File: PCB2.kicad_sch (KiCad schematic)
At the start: 8 parts, among them J701 Conn_02x03_Odd_Even

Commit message: Finish 0.1.0 design
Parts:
- J701: LCSC (none) -> C65114
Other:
- title: SH-wg -> Sailor Hat WiFi Gateway
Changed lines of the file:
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@@
   (paper "A4")
   (title_block
-    (title "SH-wg")
+    (title "Sailor Hat WiFi Gateway")
     (date "2022-01-25")
     (rev "0.1.0")
@@
     )
     (property "Datasheet" "~" (id 3) (at 132.08 60.96 0)
+      (effects (font (size 1.27 1.27)) hide)
+    )
+    (property "LCSC" "C65114" (id 4) (at 132.08 60.96 0)
       (effects (font (size 1.27 1.27)) hide)
     )
@@
     (pin "6")
   )
-  (symbol (lib_id "SH-ESP32-mini:+3V3_1") (at 147.32 55.88 0) (unit 1)
+  (symbol (lib_id "SH-wg:+3V3_1") (at 147.32 55.88 0) (unit 1)
     (in_bom yes) (on_board yes) (fields_autoplaced)
     (property "Reference" "#PWR0703" (id 0) (at 147.32 59.69 0)
@@
     (pin "1")
   )
-  (symbol (lib_id "SH-ESP32-mini:+3V3_1") (at 58.42 43.18 0) (unit 1)
+  (symbol (lib_id "SH-wg:+3V3_1") (at 58.42 43.18 0) (unit 1)
     (in_bom yes) (on_board yes) (fields_autoplaced)
     (property "Reference" "#PWR0702" (id 0) (at 58.42 46.99 0)

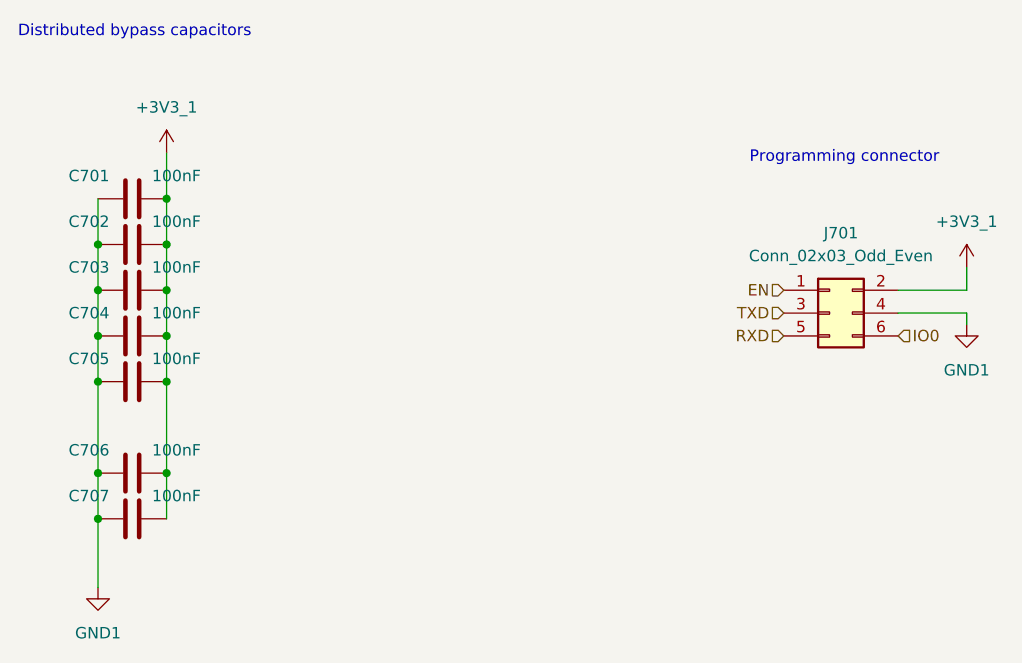
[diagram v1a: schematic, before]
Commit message: Update the design based on the test results
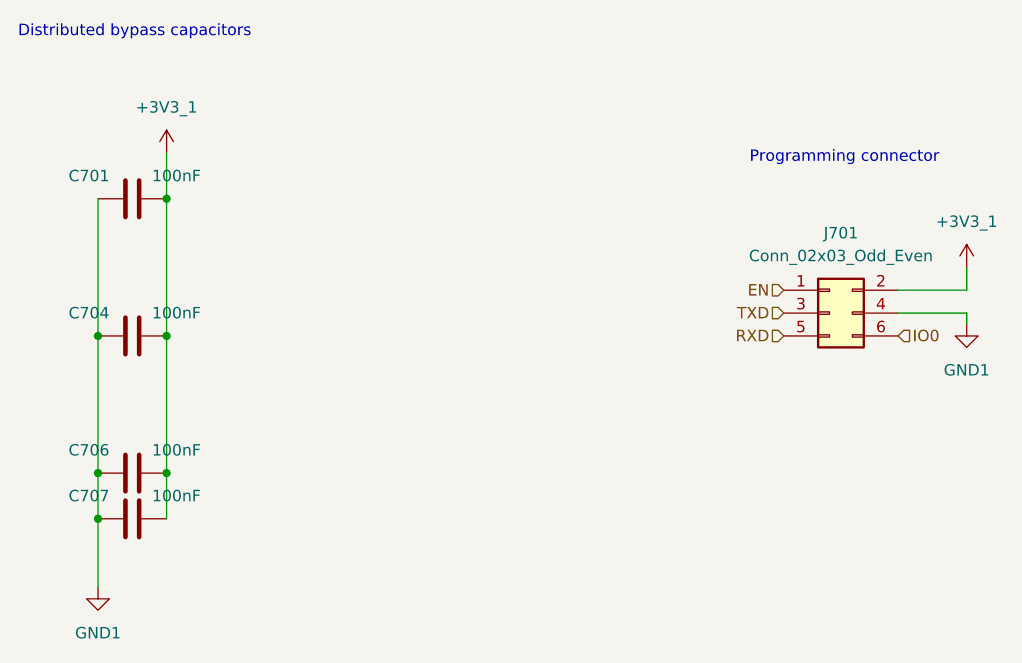
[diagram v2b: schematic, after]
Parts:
- removed C702, C703, C705: 100nF, Capacitor_SMD:C_0402_1005Metric, symbol Device:C
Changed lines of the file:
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@@
   (junction (at 50.8 63.5) (diameter 0) (color 0 0 0 0)
   )
-  (junction (at 50.8 68.58) (diameter 0) (color 0 0 0 0)
-  )
-  (junction (at 50.8 58.42) (diameter 0) (color 0 0 0 0)
-  )
   (junction (at 58.42 48.26) (diameter 0) (color 0 0 0 0)
-  )
-  (junction (at 58.42 53.34) (diameter 0) (color 0 0 0 0)
-  )
-  (junction (at 58.42 68.58) (diameter 0) (color 0 0 0 0)
   )
   (junction (at 50.8 78.74) (diameter 0) (color 0 0 0 0)
@@
   (junction (at 58.42 78.74) (diameter 0) (color 0 0 0 0)
   )
-  (junction (at 50.8 53.34) (diameter 0) (color 0 0 0 0)
-  )
   (junction (at 58.42 63.5) (diameter 0) (color 0 0 0 0)
   )
-  (junction (at 58.42 58.42) (diameter 0) (color 0 0 0 0)
-  )
-  (wire (pts (xy 50.8 58.42) (xy 50.8 63.5))
-    (stroke (width 0) (type default) (color 0 0 0 0))
-  )
-  (wire (pts (xy 58.42 53.34) (xy 58.42 48.26))
+  (wire (pts (xy 50.8 48.26) (xy 50.8 63.5))
     (stroke (width 0) (type default) (color 0 0 0 0))
   )
@@
     (stroke (width 0) (type default) (color 0 0 0 0))
   )
-  (wire (pts (xy 58.42 68.58) (xy 58.42 78.74))
+  (wire (pts (xy 58.42 63.5) (xy 58.42 78.74))
     (stroke (width 0) (type default) (color 0 0 0 0))
   )
-  (wire (pts (xy 58.42 68.58) (xy 58.42 63.5))
-    (stroke (width 0) (type default) (color 0 0 0 0))
-  )
-  (wire (pts (xy 50.8 48.26) (xy 50.8 53.34))
-    (stroke (width 0) (type default) (color 0 0 0 0))
-  )
-  (wire (pts (xy 58.42 58.42) (xy 58.42 53.34))
-    (stroke (width 0) (type default) (color 0 0 0 0))
-  )
-  (wire (pts (xy 50.8 53.34) (xy 50.8 58.42))
+  (wire (pts (xy 58.42 48.26) (xy 58.42 63.5))
     (stroke (width 0) (type default) (color 0 0 0 0))
   )
@@
     (stroke (width 0) (type default) (color 0 0 0 0))
   )
-  (wire (pts (xy 50.8 63.5) (xy 50.8 68.58))
-    (stroke (width 0) (type default) (color 0 0 0 0))
-  )
   (wire (pts (xy 147.32 60.96) (xy 139.7 60.96))
     (stroke (width 0) (type default) (color 0 0 0 0))
   )
-  (wire (pts (xy 58.42 63.5) (xy 58.42 58.42))
-    (stroke (width 0) (type default) (color 0 0 0 0))
-  )
-  (wire (pts (xy 50.8 68.58) (xy 50.8 78.74))
+  (wire (pts (xy 50.8 63.5) (xy 50.8 78.74))
     (stroke (width 0) (type default) (color 0 0 0 0))
   )
@@
   (hierarchical_label "EN" (shape input) (at 127 58.42 180)
     (effects (font (size 1.27 1.27)) (justify right))
-  )
-  (symbol (lib_id "Device:C") (at 54.61 68.58 90) (mirror x) (unit 1)
-    (in_bom yes) (on_board yes)
-    (property "Reference" "C705" (id 0) (at 52.07 66.04 90)
-      (effects (font (size 1.27 1.27)) (justify left))
-    )
-    (property "Value" "100nF" (id 1) (at 62.23 66.04 90)
-      (effects (font (size 1.27 1.27)) (justify left))
-    )
-    (property "Footprint" "Capacitor_SMD:C_0402_1005Metric" (id 2) (at 58.42 69.5452 0)
-      (effects (font (size 1.27 1.27)) hide)
-    )
-    (property "Datasheet" "~" (id 3) (at 54.61 68.58 0)
-      (effects (font (size 1.27 1.27)) hide)
-    )
-    (property "LCSC" "C1525" (id 4) (at 54.61 68.58 0)
-      (effects (font (size 1.27 1.27)) hide)
-    )
-    (pin "1")
-    (pin "2")
   )
   (symbol (lib_id "Device:C") (at 54.61 48.26 90) (mirror x) (unit 1)
@@
     (pin "2")
   )
-  (symbol (lib_id "Device:C") (at 54.61 58.42 90) (mirror x) (unit 1)
-    (in_bom yes) (on_board yes)
-    (property "Reference" "C703" (id 0) (at 52.07 55.88 90)
-      (effects (font (size 1.27 1.27)) (justify left))
-    )
-    (property "Value" "100nF" (id 1) (at 62.23 55.88 90)
-      (effects (font (size 1.27 1.27)) (justify left))
-    )
-    (property "Footprint" "Capacitor_SMD:C_0402_1005Metric" (id 2) (at 58.42 59.3852 0)
-      (effects (font (size 1.27 1.27)) hide)
-    )
-    (property "Datasheet" "~" (id 3) (at 54.61 58.42 0)
-      (effects (font (size 1.27 1.27)) hide)
-    )
-    (property "LCSC" "C1525" (id 4) (at 54.61 58.42 0)
-      (effects (font (size 1.27 1.27)) hide)
-    )
-    (pin "1")
-    (pin "2")
-  )
   (symbol (lib_id "power:GND1") (at 147.32 62.23 0) (unit 1)
     (in_bom yes) (on_board yes) (fields_autoplaced)
@@
     (pin "1")
   )
-  (symbol (lib_id "Device:C") (at 54.61 53.34 90) (mirror x) (unit 1)
-    (in_bom yes) (on_board yes)
-    (property "Reference" "C702" (id 0) (at 52.07 50.8 90)
-      (effects (font (size 1.27 1.27)) (justify left))
-    )
-    (property "Value" "100nF" (id 1) (at 62.23 50.8 90)
-      (effects (font (size 1.27 1.27)) (justify left))
-    )
-    (property "Footprint" "Capacitor_SMD:C_0402_1005Metric" (id 2) (at 58.42 54.3052 0)
-      (effects (font (size 1.27 1.27)) hide)
-    )
-    (property "Datasheet" "~" (id 3) (at 54.61 53.34 0)
-      (effects (font (size 1.27 1.27)) hide)
-    )
-    (property "LCSC" "C1525" (id 4) (at 54.61 53.34 0)
-      (effects (font (size 1.27 1.27)) hide)
-    )
-    (pin "1")
-    (pin "2")
-  )
   (symbol (lib_id "Connector_Generic:Conn_02x03_Odd_Even") (at 132.08 60.96 0) (unit 1)
